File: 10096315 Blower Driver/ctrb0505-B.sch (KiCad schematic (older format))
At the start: 87 parts

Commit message: Blower schematic: schematic and layout synchro
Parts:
- V1, V10, V11, V12, V13, V15, V16, V19, V2, V20, V22, V23, V26, V27, V28, V29, V31, V32, V33, V35, V38, V39, V41, V42, V43, V47, V50, V52, V64, V66, V67, V68, V69, V7, V70, V75, V76, V77, V78, V79, V8, V80, V81, V82, V84: footprint batt:VIA-100X04-VE -> save10096315 Blower Driver:VIA-091X03-VE_1010
- V14, V17, V18, V21, V24, V25, V30, V34, V36, V37, V40, V48, V49, V51, V54, V55, V56, V57, V58, V59, V61, V62, V63, V71, V72, V73, V74, V83, V9: footprint batt:VIA-100X04-VE -> save10096315 Blower Driver:VIA-091X03-VE_1100
- V3, V44, V45, V65, V85, V86, V87: footprint batt:VIA-100X04-VE -> save10096315 Blower Driver:VIA-091X03-VE_1001
- V4, V5, V6: footprint batt:VIA-100X04-VE -> save10096315 Blower Driver:VIA-091X03-VE_0011
- V46, V53, V60: footprint batt:VIA-100X04-VE -> save10096315 Blower Driver:VIA-091X03-VE_1101

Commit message: Blower: library and project update from last pcb file
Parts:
- V1, V10, V11, V12, V13, V15, V16, V19, V2, V20, V22, V23, V26, V27, V28, V29, V31, V32, V33, V35, V38, V39, V41, V42, V43, V47, V50, V52, V64, V66, V67, V68, V69, V7, V70, V75, V76, V77, V78, V79, V8, V80, V81, V82, V84: footprint save10096315 Blower Driver:VIA-091X03-VE_1010 -> 10096315 Blower Driver:VIA-091X03-VE_1011
- V14, V17, V18, V21, V24, V25, V30, V34, V36, V37, V40, V48, V49, V51, V54, V55, V56, V57, V58, V59, V61, V62, V63, V71, V72, V73, V74, V83, V9: footprint save10096315 Blower Driver:VIA-091X03-VE_1100 -> 10096315 Blower Driver:VIA-091X03-VE_1101
- V3, V44, V45, V65, V85, V86, V87: footprint save10096315 Blower Driver:VIA-091X03-VE_1001 -> 10096315 Blower Driver:VIA-091X03-VE_1001
- V4, V5, V6: footprint save10096315 Blower Driver:VIA-091X03-VE_0011 -> 10096315 Blower Driver:VIA-091X03-VE_1011
- V46, V53, V60: footprint save10096315 Blower Driver:VIA-091X03-VE_1101 -> 10096315 Blower Driver:VIA-091X03-VE_1101

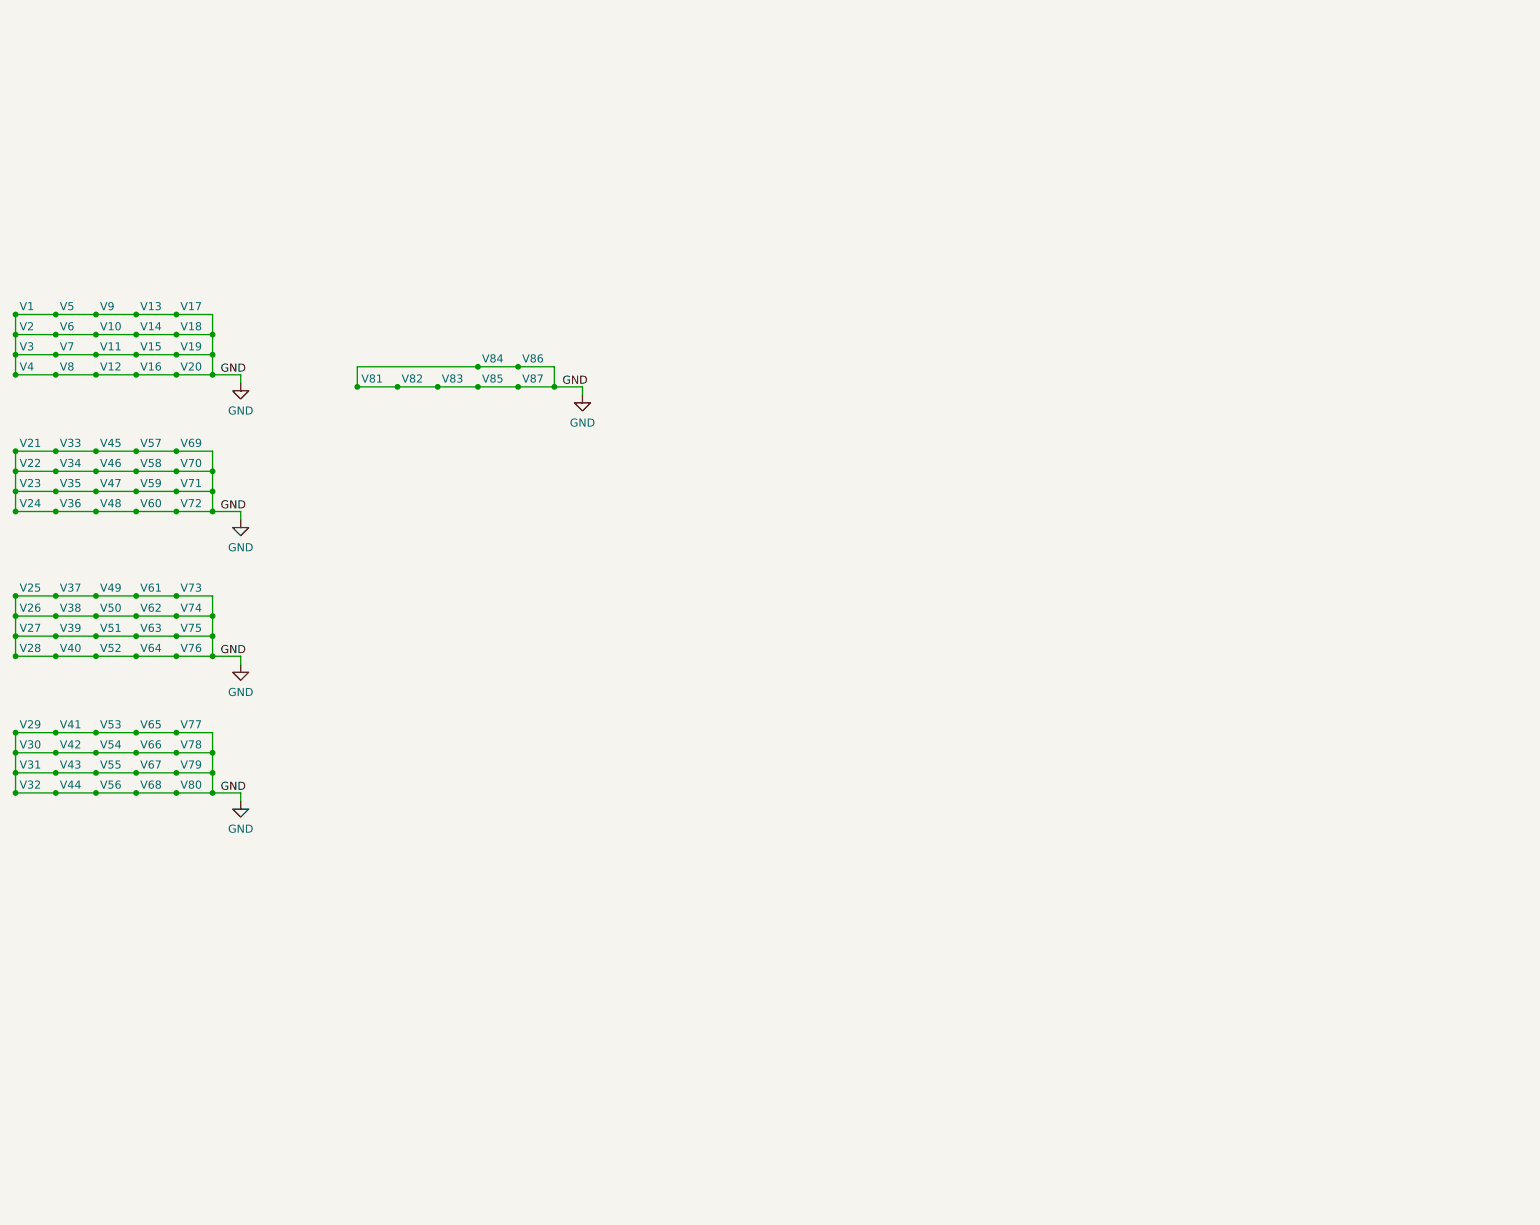
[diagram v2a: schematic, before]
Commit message: Add vias names on schematics
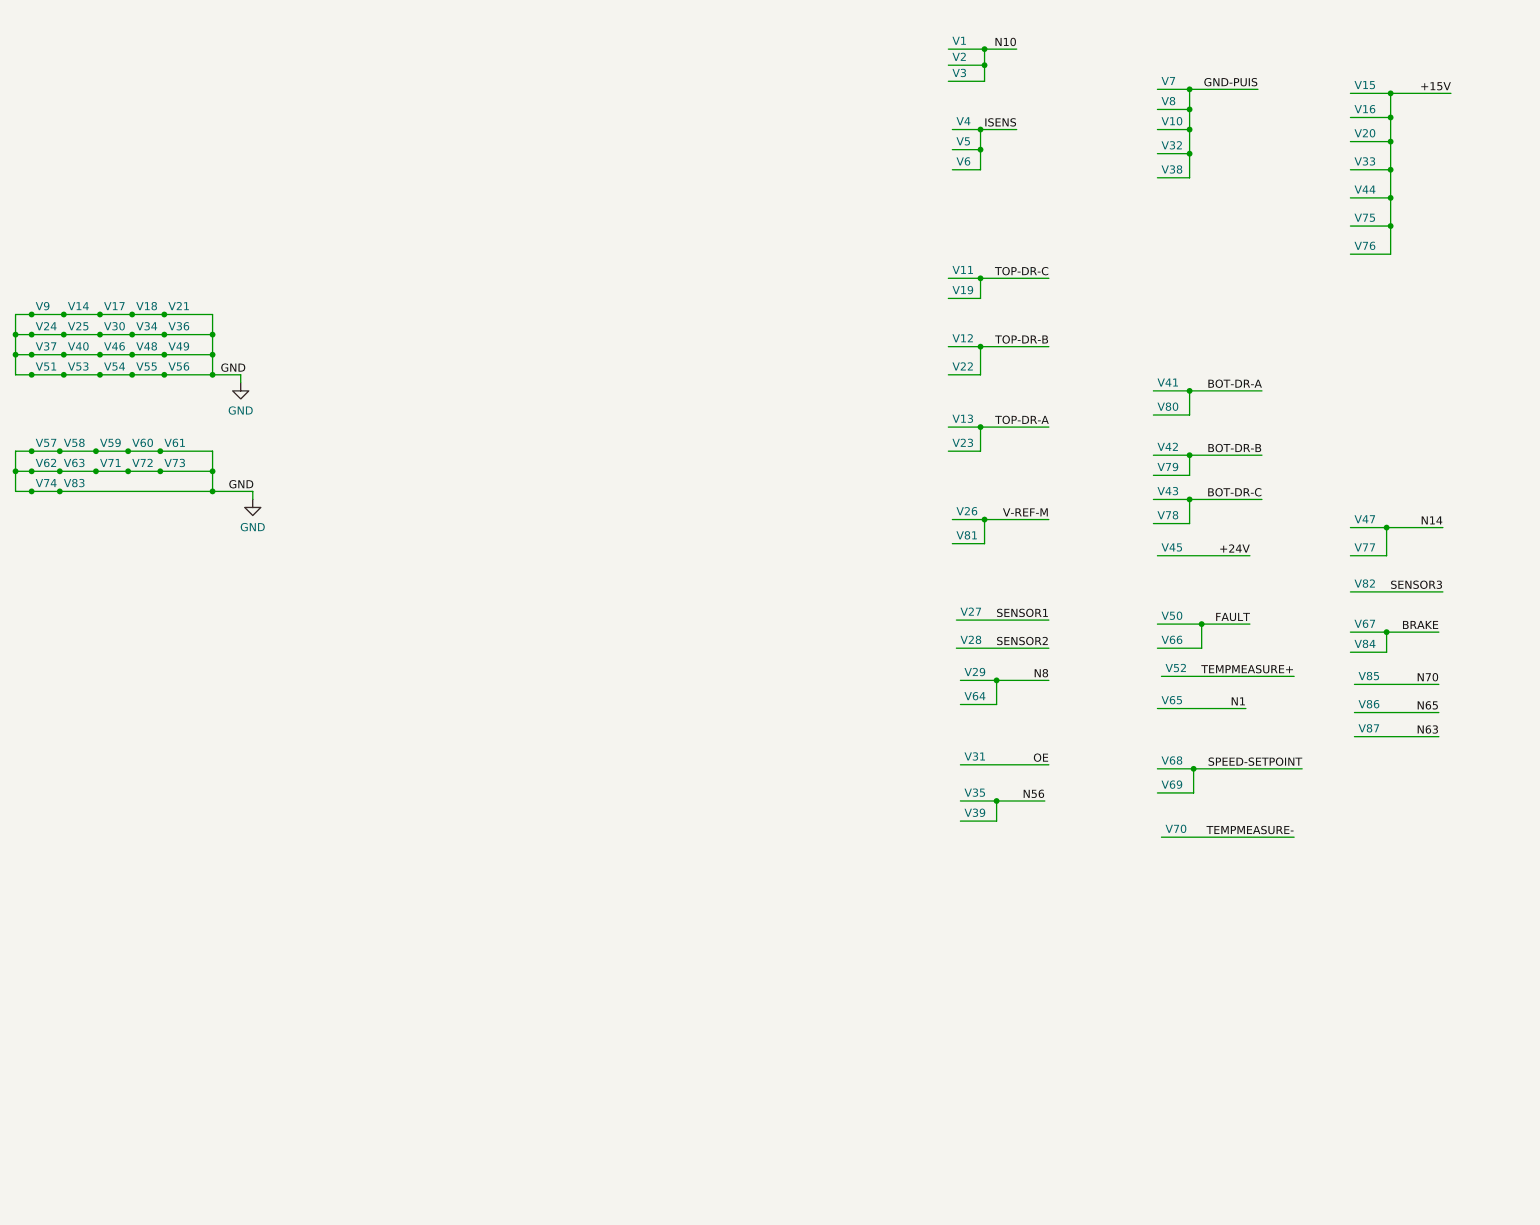
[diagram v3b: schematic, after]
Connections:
- net GND: no longer V1.~, V10.~, V11.~, V12.~, V13.~, V15.~, V16.~, V19.~, V2.~, V20.~, V22.~, V23.~, V26.~, V27.~, V28.~, V29.~, V3.~, V31.~, V32.~, V33.~, V35.~, V38.~, V39.~, V4.~, V41.~, V42.~, V43.~, V44.~, V45.~, V47.~, V5.~, V50.~, V52.~, V6.~, V64.~, V65.~, V66.~, V67.~, V68.~, V69.~, V7.~, V70.~, V75.~, V76.~, V77.~, V78.~, V79.~, V8.~, V80.~, V81.~, V82.~, V84.~, V85.~, V86.~, V87.~
- new net +15V: V15.~, V16.~, V20.~, V33.~, V44.~, V75.~, V76.~
- new net +24V: V45.~
- new net BOT-DR-A: V41.~, V80.~
- new net BOT-DR-B: V42.~, V79.~
- new net BOT-DR-C: V43.~, V78.~
- new net BRAKE: V67.~, V84.~
- new net FAULT: V50.~, V66.~
- new net GND-PUIS: V10.~, V32.~, V38.~, V7.~, V8.~
- new net ISENS: V4.~, V5.~, V6.~
- new net N1: V65.~
- new net N10: V1.~, V2.~, V3.~
- new net N14: V47.~, V77.~
- new net N56: V35.~, V39.~
- new net N63: V87.~
- new net N65: V86.~
- new net N70: V85.~
- new net N8: V29.~, V64.~
- new net OE: V31.~
- new net SENSOR1: V27.~
- new net SENSOR2: V28.~
- new net SENSOR3: V82.~
- new net SPEED-SETPOINT: V68.~, V69.~
- new net TEMPMEASURE+: V52.~
- new net TEMPMEASURE-: V70.~
- new net TOP-DR-A: V13.~, V23.~
- new net TOP-DR-B: V12.~, V22.~
- new net TOP-DR-C: V11.~, V19.~
- new net V-REF-M: V26.~, V81.~

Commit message: Rename net names on schematics part 2
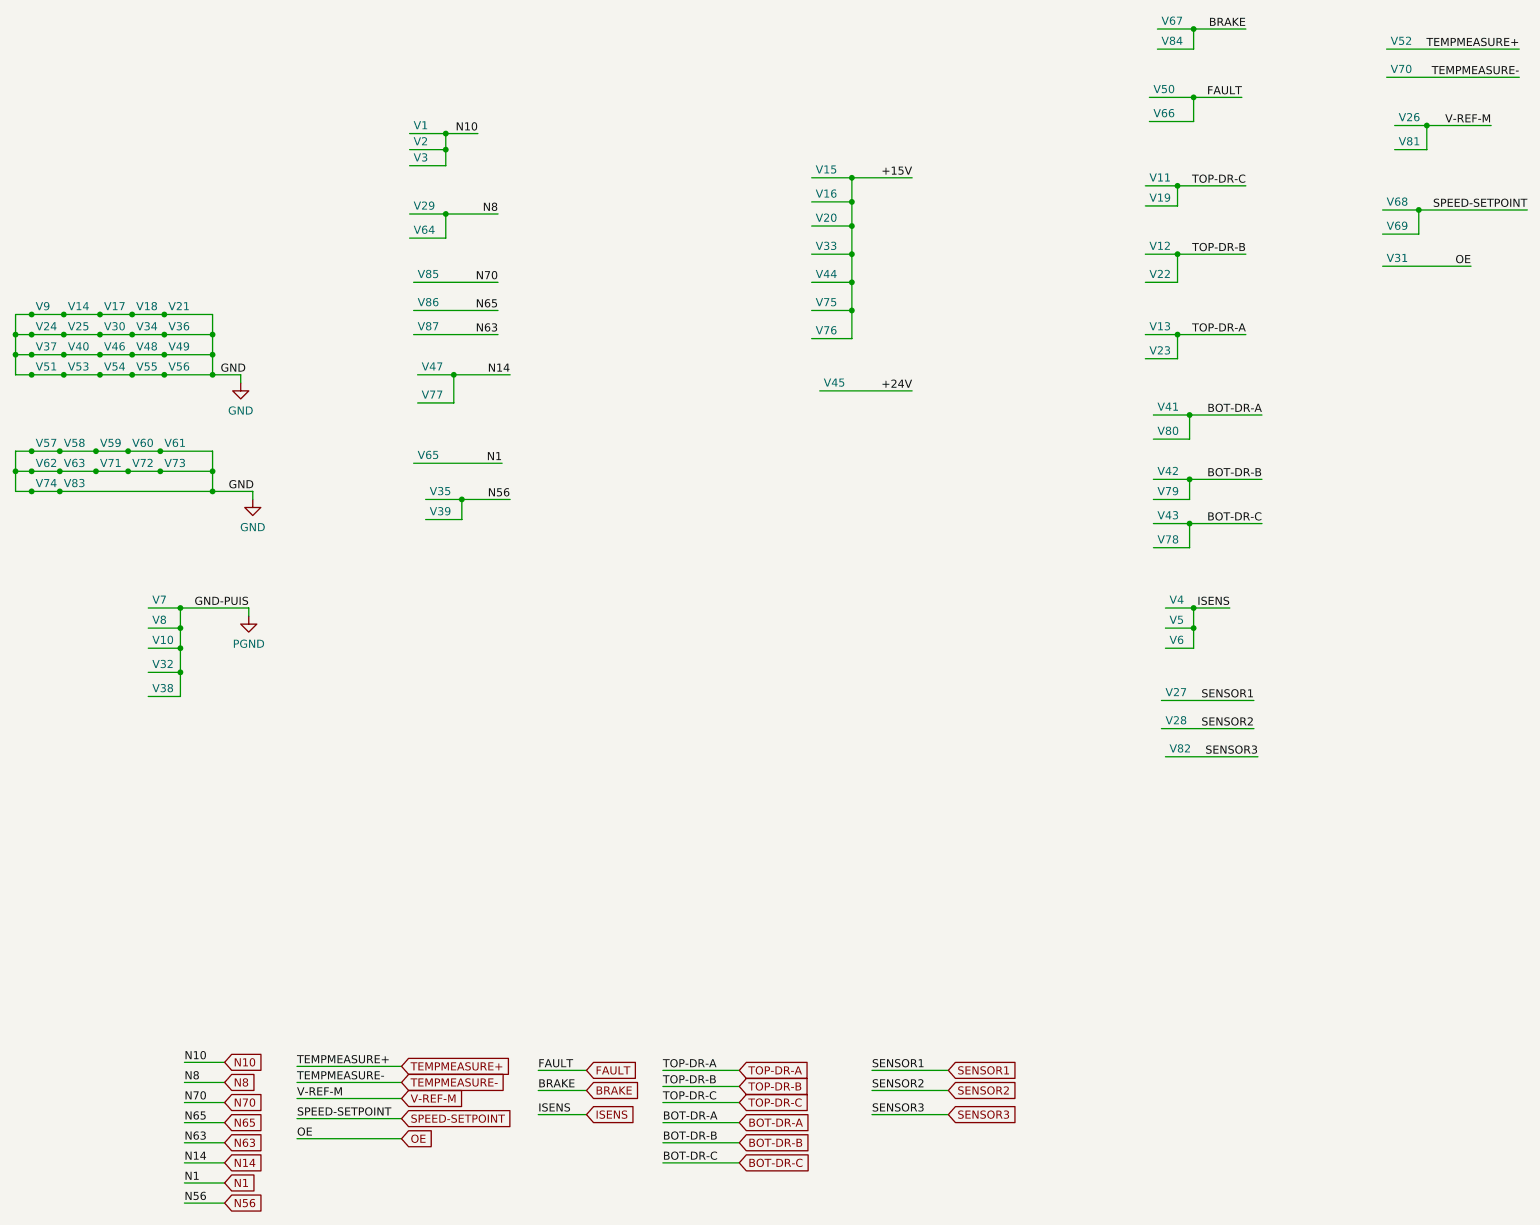
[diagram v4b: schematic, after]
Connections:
- net GND-PUIS renamed PGND

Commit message: Replace backslash by tilde for negative signals
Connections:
- net BRAKE renamed ~BRAKE~
- net FAULT renamed ~FAULT~
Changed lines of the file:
@@
 	8175 1325 8450 1325
 Text Label 8750 1325 2    50   ~ 0
-FAULT
+~FAULT~
 Wire Wire Line
 	9650 1025 10475 1025
@@
 	8225 900  8450 900
 Text Label 8775 900  2    50   ~ 0
-BRAKE
+~BRAKE~
 Wire Wire Line
 	9625 2025 9850 2025
@@
 	2575 4550 2575 4500
 Text Label 4375 7375 0    50   ~ 0
-FAULT
+~FAULT~
 Wire Wire Line
 	4375 7375 4675 7375
 Text GLabel 4675 7375 2    50   Input ~ 0
-FAULT
+~FAULT~
 Text Label 4375 7500 0    50   ~ 0
-BRAKE
+~BRAKE~
 Wire Wire Line
 	4375 7500 4675 7500
 Text GLabel 4675 7500 2    50   Input ~ 0
-BRAKE
+~BRAKE~
 Text Label 4375 7650 0    50   ~ 0
 ISENS

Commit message: Blower episode 4
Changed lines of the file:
@@
 Text GLabel 3525 7350 2    50   Input ~ 0
 TEMPMEASURE+
-Text GLabel 3525 7800 2    50   Input ~ 0
+Text GLabel 4675 7825 2    50   Input ~ 0
 OE
 Text GLabel 2425 7325 2    50   Input ~ 0
@@
 SPEED-SETPOINT
 Wire Wire Line
-	3525 7800 2875 7800
+	4675 7825 4475 7825
 Wire Wire Line
 	2425 7325 2175 7325
-Text Label 2875 7800 0    50   ~ 0
+Text Label 4475 7825 0    50   ~ 0
 OE
 Text Label 2175 7325 0    50   ~ 0
@@
 Text Label 2175 8200 0    50   ~ 0
 N56
+Text GLabel 4675 8150 2    50   Input ~ 0
+GND-PUIS
+Wire Wire Line
+	4675 8150 4275 8150
+Text Label 4275 8150 0    50   ~ 0
+GND-PUIS
 $EndSCHEMATC

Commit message: Blower episode 6 Schematics and Layout fully synchronized
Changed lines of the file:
@@
 	1    0    0    -1
 $EndComp
-Text Label 2400 3050 0    50   ~ 0
-GND
 Wire Wire Line
 	2350 2675 2350 2800
@@
 	1    0    0    -1
 $EndComp
-Text Label 2450 3775 0    50   ~ 0
-GND
 Wire Wire Line
 	2350 3525 2350 3650
